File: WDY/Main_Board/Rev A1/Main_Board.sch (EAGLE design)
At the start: 191 parts, among them J1 22-05-7028-02, J10 22-05-7038-03, J11 22-05-7028-02, J12 22-05-7028-02, J13 22-05-7028-02, J14 22-05-7028-02, J15 22-05-7058-05, J16 22-27-2061-06, J2 22-05-7028-02, J3 22-05-7048-04, J4 22-05-7048-04, J5 1241050-5, J6 90814-0208, J7 90814-0206, J8 90814-0208, J9 22-05-7038-03, K1 G6K-2G-Y, K2 G6K-2G-Y, K3 G6K-2G-Y, K4 G6K-2G-Y, P1 RB1-125BAG1A, SW1 B3FS-1015, SW2 B3FS-1015, T1 MMBT2222AL, U1 LPC1768FBD100, U11 SN74LVC3G17DCTR, U2 SN74LVC3G17DCTR, U3 SN74LVC3G17DCTR, U4 TPL0401A, U5 AT24C512C-SSHM-B, U6 SN74LVC2G17DBVR, U7 SN74LVC2G17DBVR, U8 LT1767EMS8E-5PBF, U9 TC1264-3.3, X1 FC-135, X2 MSTBA2

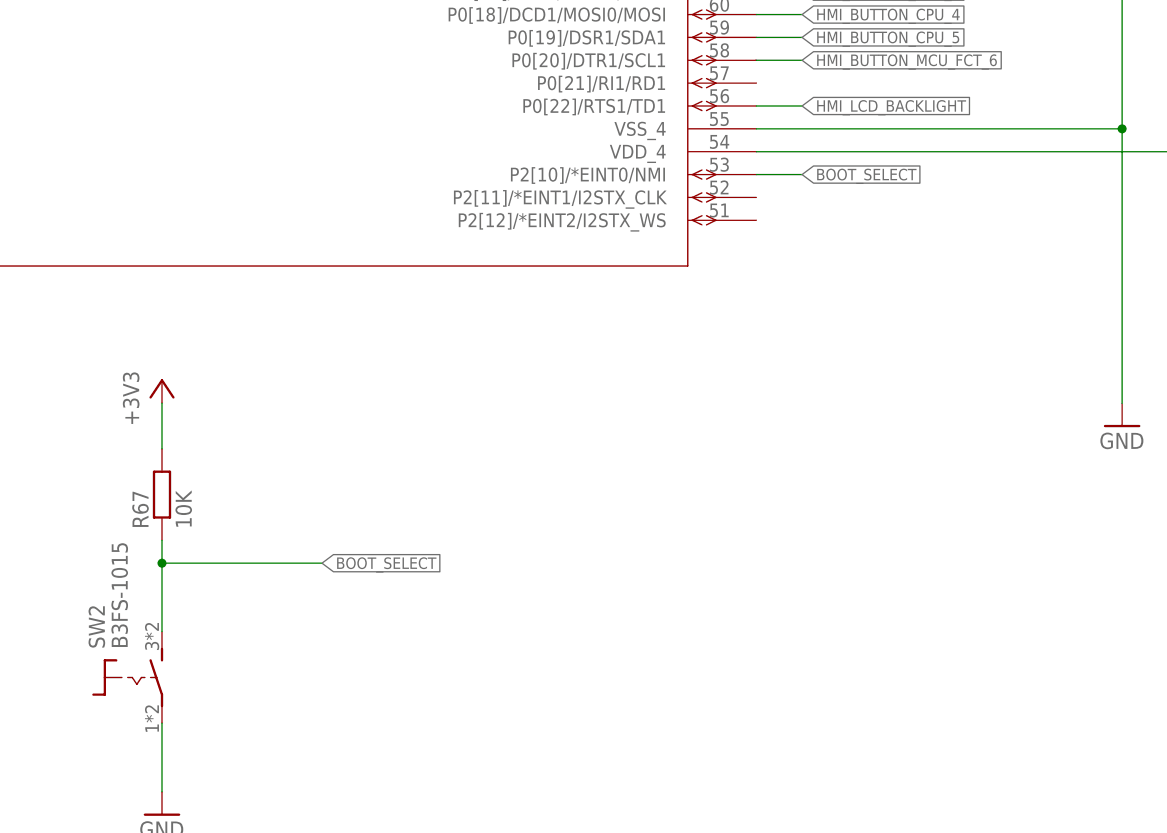
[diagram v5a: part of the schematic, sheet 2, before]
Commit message: Fix : BOOT_SELECT signal must be configurable to P2_10 and P2_12
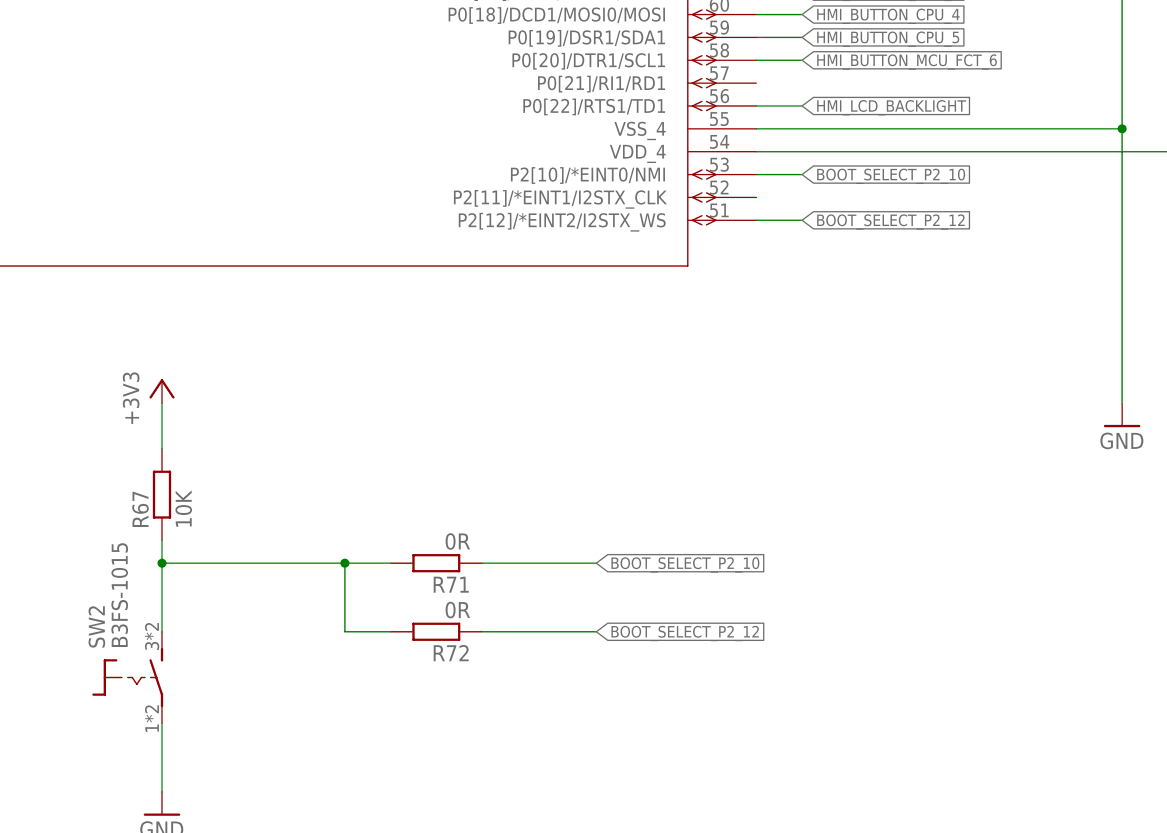
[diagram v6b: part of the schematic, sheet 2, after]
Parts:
- added R71, R72: 0R, rcl:R-EU_R0603
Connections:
- removed net BOOT_SELECT: R67.1, SW2.1, U1.P2[10]/*EINT0/NMI
- new net BOOT_SELECT_P2_10: R71.1, U1.P2[10]/*EINT0/NMI
- new net BOOT_SELECT_P2_12: R72.1, U1.P2[12]/*EINT2/I2STX_WS
- new net N$5: R67.1, R71.2, R72.2, SW2.1
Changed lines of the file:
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@@
 <part name="TP3" library="testpad" deviceset="TP" device="B1,27"/>
 <part name="JP1" library="exmachina" deviceset="BC-2-?" device="P"/>
+<part name="R71" library="rcl" deviceset="R-EU_" device="R0603" value="0R"/>
+<part name="R72" library="rcl" deviceset="R-EU_" device="R0603" value="0R"/>
 </parts>
 <sheets>
@@
 <instance part="GND89" gate="1" x="58.42" y="93.98"/>
 <instance part="JP1" gate="G$1" x="60.96" y="63.5"/>
+<instance part="R71" gate="G$1" x="279.4" y="71.12" rot="R180"/>
+<instance part="R72" gate="G$1" x="279.4" y="63.5" rot="R180"/>
 </instances>
 <busses>
@@
 </segment>
 </net>
-<net name="BOOT_SELECT" class="1">
-<segment>
-<pinref part="U1" gate="A" pin="P2[10]/*EINT0/NMI"/>
-<wire x1="314.96" y1="114.3" x2="320.04" y2="114.3" width="0.1524" layer="91"/>
-<label x="320.04" y="114.3" size="1.27" layer="95" xref="yes"/>
-</segment>
-<segment>
-<pinref part="R67" gate="G$1" pin="1"/>
-<pinref part="SW2" gate="G$1" pin="1"/>
-<wire x1="248.92" y1="73.66" x2="248.92" y2="71.12" width="0.1524" layer="91"/>
-<wire x1="248.92" y1="71.12" x2="248.92" y2="63.5" width="0.1524" layer="91"/>
-<wire x1="248.92" y1="71.12" x2="266.7" y2="71.12" width="0.1524" layer="91"/>
-<junction x="248.92" y="71.12"/>
-<label x="266.7" y="71.12" size="1.27" layer="95" xref="yes"/>
-</segment>
-</net>
 <net name="EEPROM_SDA" class="0">
 <segment>
@@
 </segment>
 </net>
+<net name="N$5" class="1">
+<segment>
+<pinref part="SW2" gate="G$1" pin="1"/>
+<pinref part="R67" gate="G$1" pin="1"/>
+<wire x1="248.92" y1="73.66" x2="248.92" y2="71.12" width="0.1524" layer="91"/>
+<pinref part="R71" gate="G$1" pin="2"/>
+<wire x1="248.92" y1="71.12" x2="248.92" y2="63.5" width="0.1524" layer="91"/>
+<wire x1="274.32" y1="71.12" x2="269.24" y2="71.12" width="0.1524" layer="91"/>
+<junction x="248.92" y="71.12"/>
+<pinref part="R72" gate="G$1" pin="2"/>
+<wire x1="269.24" y1="71.12" x2="248.92" y2="71.12" width="0.1524" layer="91"/>
+<wire x1="274.32" y1="63.5" x2="269.24" y2="63.5" width="0.1524" layer="91"/>
+<wire x1="269.24" y1="63.5" x2="269.24" y2="71.12" width="0.1524" layer="91"/>
+<junction x="269.24" y="71.12"/>
+</segment>
+</net>
+<net name="BOOT_SELECT_P2_12" class="1">
+<segment>
+<pinref part="R72" gate="G$1" pin="1"/>
+<wire x1="284.48" y1="63.5" x2="297.18" y2="63.5" width="0.1524" layer="91"/>
+<label x="297.18" y="63.5" size="1.27" layer="95" xref="yes"/>
+</segment>
+<segment>
+<pinref part="U1" gate="A" pin="P2[12]/*EINT2/I2STX_WS"/>
+<wire x1="314.96" y1="109.22" x2="320.04" y2="109.22" width="0.1524" layer="91"/>
+<label x="320.04" y="109.22" size="1.27" layer="95" xref="yes"/>
+</segment>
+</net>
+<net name="BOOT_SELECT_P2_10" class="1">
+<segment>
+<label x="297.18" y="71.12" size="1.27" layer="95" xref="yes"/>
+<pinref part="R71" gate="G$1" pin="1"/>
+<wire x1="284.48" y1="71.12" x2="297.18" y2="71.12" width="0.1524" layer="91"/>
+</segment>
+<segment>
+<pinref part="U1" gate="A" pin="P2[10]/*EINT0/NMI"/>
+<wire x1="314.96" y1="114.3" x2="320.04" y2="114.3" width="0.1524" layer="91"/>
+<label x="320.04" y="114.3" size="1.27" layer="95" xref="yes"/>
+</segment>
+</net>

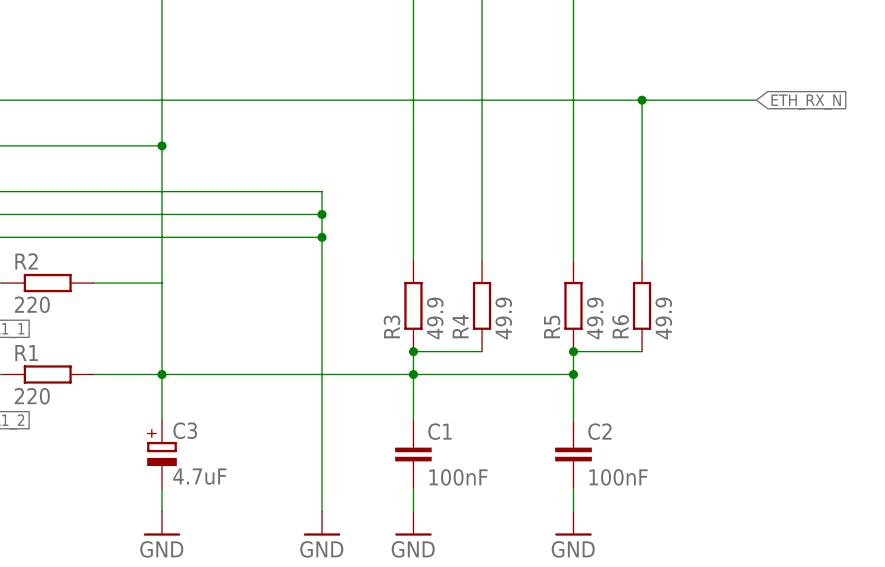
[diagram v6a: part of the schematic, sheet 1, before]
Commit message: Fix :  Ethernet filters connection misleading
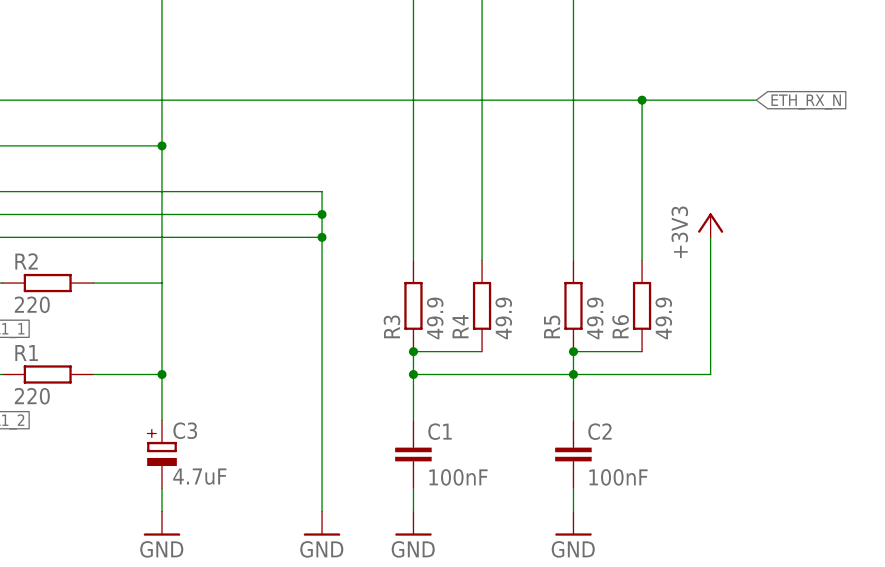
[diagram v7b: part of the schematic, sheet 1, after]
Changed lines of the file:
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@@
 <part name="R71" library="rcl" deviceset="R-EU_" device="R0603" value="0R"/>
 <part name="R72" library="rcl" deviceset="R-EU_" device="R0603" value="0R"/>
+<part name="+3V30" library="supply1" deviceset="+3V3" device=""/>
 </parts>
 <sheets>
@@
 <instance part="P+21" gate="1" x="96.52" y="83.82"/>
 <instance part="GND51" gate="1" x="360.68" y="124.46"/>
+<instance part="+3V30" gate="G$1" x="139.7" y="193.04"/>
 </instances>
 <busses>
@@
 <net name="+3V3" class="2">
 <segment>
-<pinref part="R2" gate="G$1" pin="2"/>
 <pinref part="C3" gate="G$1" pin="+"/>
-<wire x1="71.12" y1="185.42" x2="78.74" y2="185.42" width="0.1524" layer="91"/>
-<wire x1="78.74" y1="185.42" x2="78.74" y2="175.26" width="0.1524" layer="91"/>
 <pinref part="+3V1" gate="G$1" pin="+3V3"/>
-<wire x1="78.74" y1="175.26" x2="78.74" y2="170.18" width="0.1524" layer="91"/>
-<wire x1="78.74" y1="185.42" x2="78.74" y2="200.66" width="0.1524" layer="91"/>
+<wire x1="78.74" y1="200.66" x2="78.74" y2="248.92" width="0.1524" layer="91"/>
 <pinref part="P1" gate="G$1" pin="CT"/>
-<wire x1="78.74" y1="200.66" x2="78.74" y2="248.92" width="0.1524" layer="91"/>
 <wire x1="53.34" y1="200.66" x2="78.74" y2="200.66" width="0.1524" layer="91"/>
 <junction x="78.74" y="200.66"/>
+<pinref part="R2" gate="G$1" pin="2"/>
+<wire x1="71.12" y1="185.42" x2="78.74" y2="185.42" width="0.1524" layer="91"/>
+<wire x1="78.74" y1="185.42" x2="78.74" y2="200.66" width="0.1524" layer="91"/>
+<wire x1="78.74" y1="185.42" x2="78.74" y2="175.26" width="0.1524" layer="91"/>
+<wire x1="78.74" y1="175.26" x2="78.74" y2="170.18" width="0.1524" layer="91"/>
 <pinref part="R1" gate="G$1" pin="2"/>
 <wire x1="71.12" y1="175.26" x2="78.74" y2="175.26" width="0.1524" layer="91"/>
 <junction x="78.74" y="175.26"/>
+</segment>
+<segment>
 <pinref part="C1" gate="G$1" pin="1"/>
 <pinref part="R3" gate="G$1" pin="1"/>
@@
 <wire x1="106.68" y1="177.8" x2="114.3" y2="177.8" width="0.1524" layer="91"/>
 <junction x="106.68" y="177.8"/>
-<wire x1="78.74" y1="175.26" x2="106.68" y2="175.26" width="0.1524" layer="91"/>
 <junction x="106.68" y="175.26"/>
 <pinref part="C2" gate="G$1" pin="1"/>
@@
 <wire x1="106.68" y1="175.26" x2="124.46" y2="175.26" width="0.1524" layer="91"/>
 <junction x="124.46" y="175.26"/>
-</segment>
-<segment>
+<pinref part="+3V30" gate="G$1" pin="+3V3"/>
+<wire x1="124.46" y1="175.26" x2="139.7" y2="175.26" width="0.1524" layer="91"/>
+<wire x1="139.7" y1="175.26" x2="139.7" y2="190.5" width="0.1524" layer="91"/>
+</segment>
+<segment>

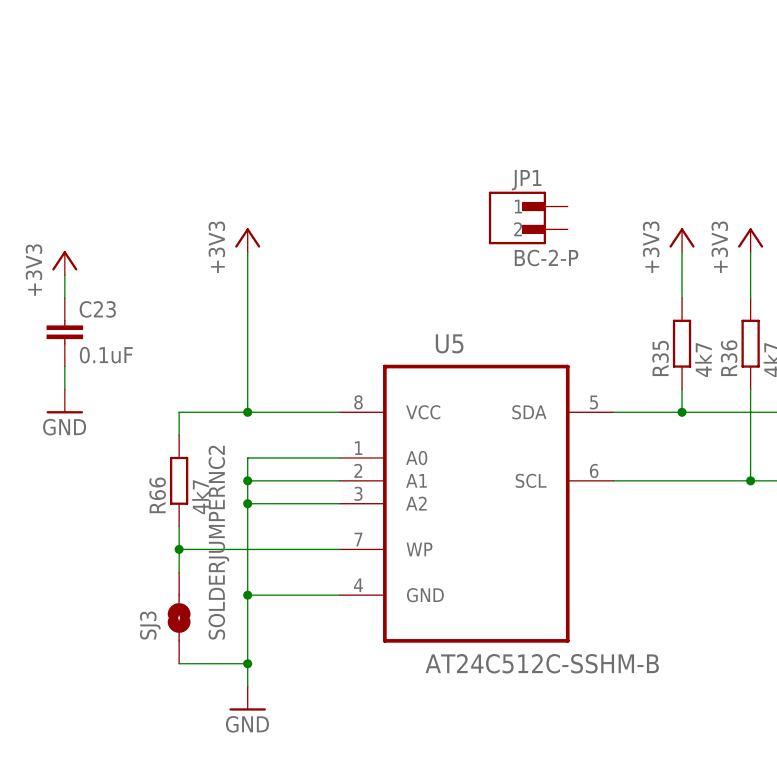
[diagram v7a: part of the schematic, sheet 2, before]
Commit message: Fix : Test pad instead of solder jumper for WP (@2.E1) // Use BC-2-P in exmachina.lbr as a test
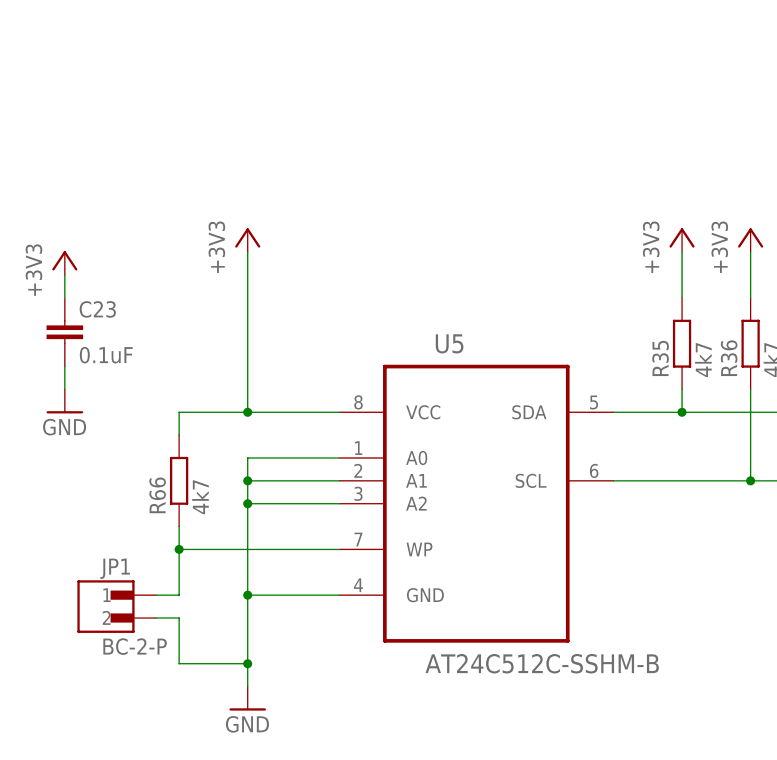
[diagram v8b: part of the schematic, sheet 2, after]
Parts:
- removed SJ3: SOLDERJUMPERNC2, SparkFun-Passives:SOLDERJUMPERNC2
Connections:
- net GND: now also JP1.2; no longer SJ3.1
- net N$22: now also JP1.1; no longer SJ3.2
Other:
- moved on the sheet: JP1
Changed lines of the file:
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@@
 <part name="GND51" library="supply1" deviceset="GND" device=""/>
 <part name="R66" library="rcl" deviceset="R-EU_" device="R0603" value="4k7"/>
-<part name="SJ3" library="SparkFun-Passives" deviceset="SOLDERJUMPER" device="NC2"/>
 <part name="U$10" library="crystal" deviceset="ASE" device="" value="ASE-12"/>
 <part name="GND52" library="supply1" deviceset="GND" device=""/>
@@
 <instance part="+3V34" gate="G$1" x="10.16" y="187.96"/>
 <instance part="R66" gate="G$1" x="22.86" y="33.02" rot="R90"/>
-<instance part="SJ3" gate="1" x="22.86" y="17.78" rot="R90"/>
 <instance part="U$10" gate="G$1" x="43.18" y="144.78"/>
 <instance part="GND52" gate="1" x="58.42" y="132.08"/>
@@
 <instance part="U$14" gate="A" x="58.42" y="104.14" rot="R90"/>
 <instance part="GND89" gate="1" x="58.42" y="93.98"/>
-<instance part="JP1" gate="G$1" x="60.96" y="63.5"/>
+<instance part="JP1" gate="G$1" x="15.24" y="20.32"/>
 <instance part="R71" gate="G$1" x="279.4" y="71.12" rot="R180"/>
 <instance part="R72" gate="G$1" x="279.4" y="63.5" rot="R180"/>
@@
 <wire x1="40.64" y1="30.48" x2="30.48" y2="30.48" width="0.1524" layer="91"/>
 <junction x="30.48" y="30.48"/>
-<pinref part="SJ3" gate="1" pin="1"/>
+<junction x="30.48" y="12.7"/>
+<pinref part="JP1" gate="G$1" pin="2"/>
+<wire x1="20.32" y1="17.78" x2="22.86" y2="17.78" width="0.1524" layer="91"/>
+<wire x1="22.86" y1="17.78" x2="22.86" y2="12.7" width="0.1524" layer="91"/>
 <wire x1="22.86" y1="12.7" x2="30.48" y2="12.7" width="0.1524" layer="91"/>
-<junction x="30.48" y="12.7"/>
 </segment>
 <segment>
@@
 <wire x1="22.86" y1="27.94" x2="22.86" y2="25.4" width="0.1524" layer="91"/>
 <wire x1="22.86" y1="25.4" x2="40.64" y2="25.4" width="0.1524" layer="91"/>
-<pinref part="SJ3" gate="1" pin="2"/>
-<wire x1="22.86" y1="22.86" x2="22.86" y2="25.4" width="0.1524" layer="91"/>
 <junction x="22.86" y="25.4"/>
-</segment>
-</net>
+<pinref part="JP1" gate="G$1" pin="1"/>
+<wire x1="20.32" y1="20.32" x2="22.86" y2="20.32" width="0.1524" layer="91"/>
+<wire x1="22.86" y1="20.32" x2="22.86" y2="25.4" width="0.1524" layer="91"/>
+</segment>
+</net>
